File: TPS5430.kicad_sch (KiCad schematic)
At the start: 41 parts, among them J1 Barrel_Jack, J2 Screw_Terminal_01x02, Q1 AO3401A, Q2 MMBT3904, U1 TPS5430DDA

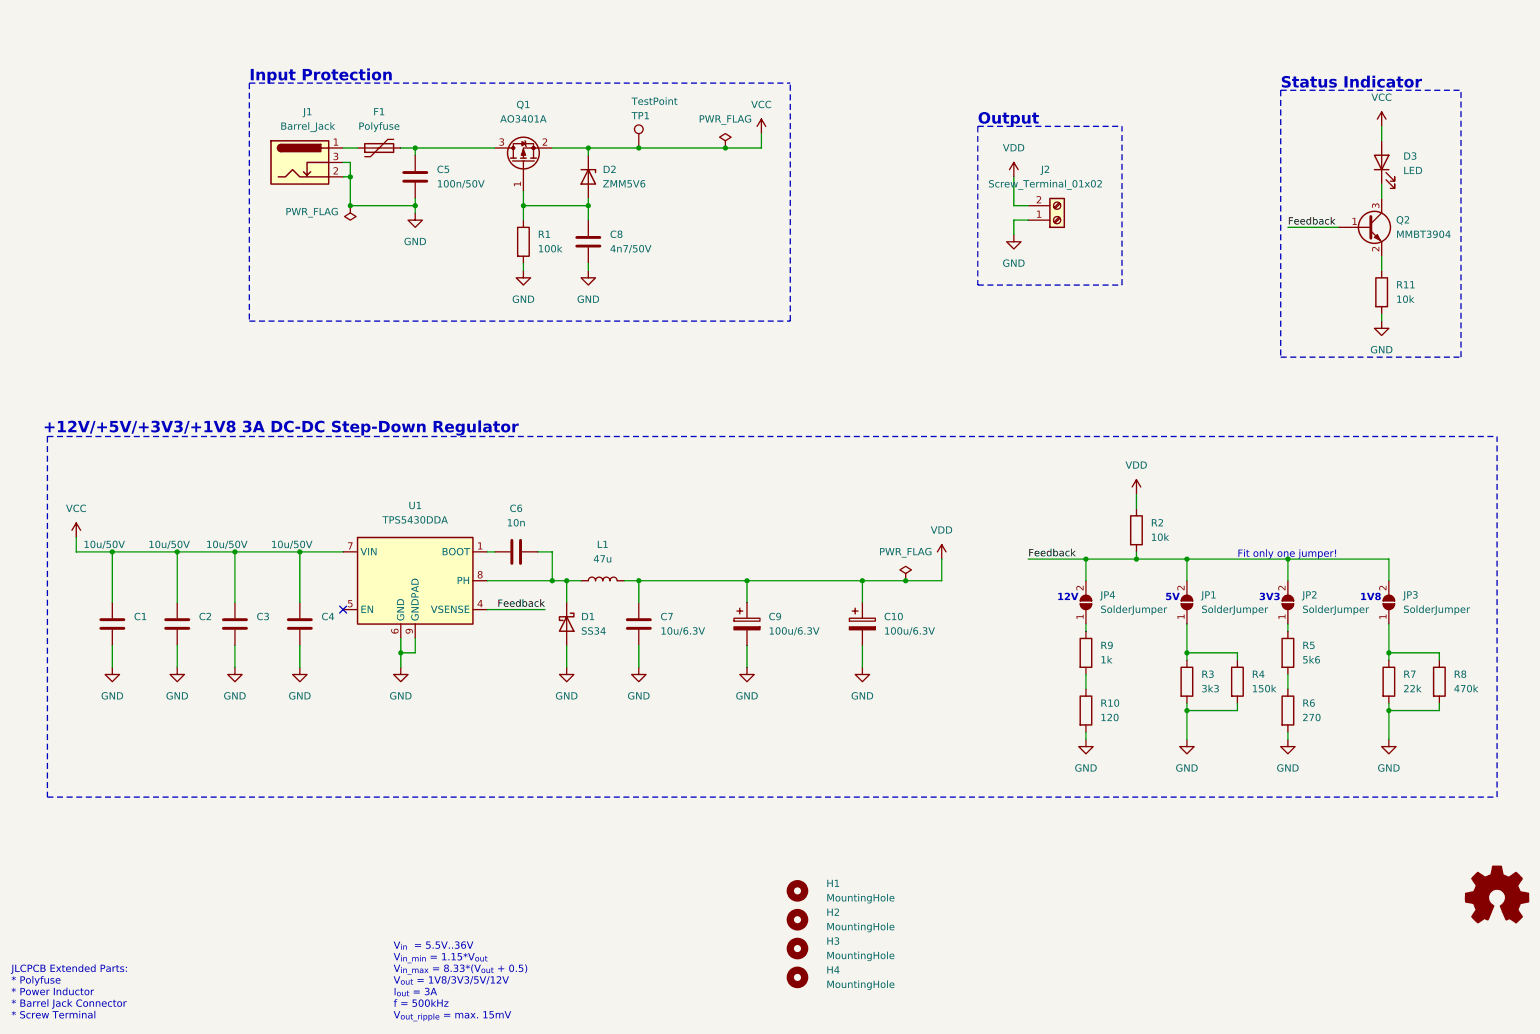
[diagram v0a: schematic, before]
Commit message: Initial addition of variable feedback block
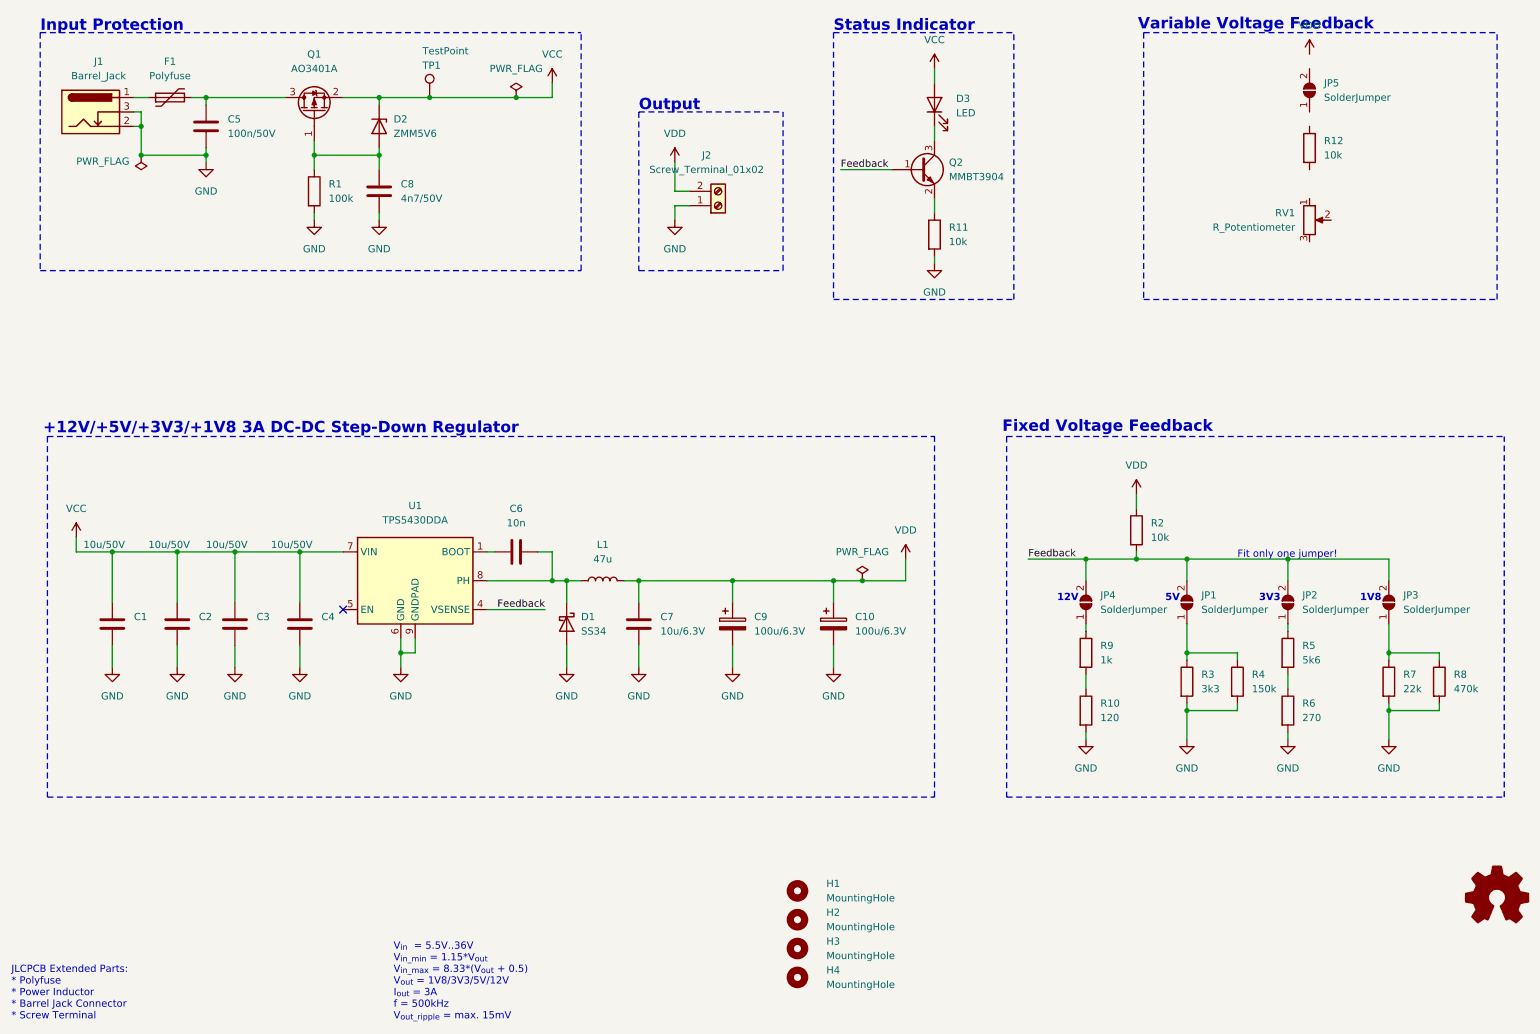
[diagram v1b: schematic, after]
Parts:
- added JP5: SolderJumper, Jumper:SolderJumper-2_P1.3mm_Open_RoundedPad1.0x1.5mm, symbol Jumper:SolderJumper_2_Open
- added R12: 10k, Resistor_SMD:R_0402_1005Metric, symbol Device:R
- added RV1: R_Potentiometer, Potentiometer_THT:Potentiometer_Bourns_3296W_Vertical, symbol Device:R_Potentiometer
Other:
- note added: "Fixed Voltage Feedback"
- note added: "Variable Voltage Feedback"
- company: Max Stabel -> Oren's Lab
- title: TPS5430 -> tps5430-variable
- moved on the sheet: C10, C5, C8, C9, D2, D3, F1, J1, J2, Q1, Q2, R1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

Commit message: Finished variable feedback block
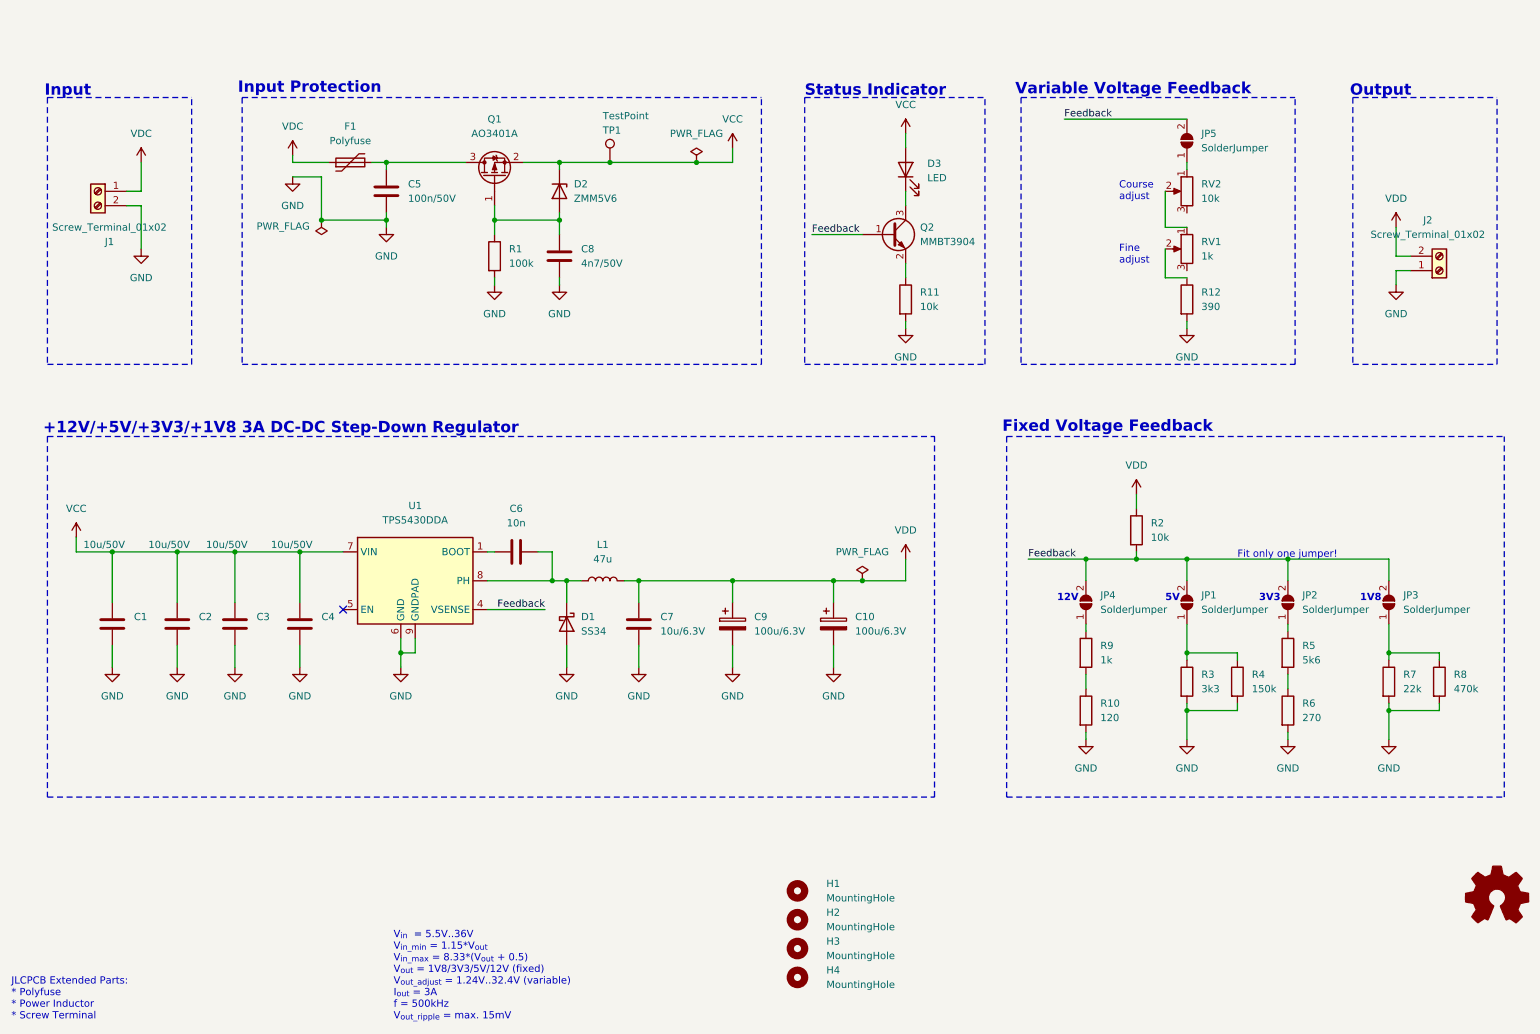
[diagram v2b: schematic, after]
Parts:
- removed J1: Barrel_Jack, tps5430:DC-005-5A-2.0-SMT, symbol Connector:Barrel_Jack_Switch
- added J1: Screw_Terminal_01x02, TerminalBlock_Phoenix:TerminalBlock_Phoenix_PT-1,5-2-3.5-H_1x02_P3.50mm_Horizontal, symbol Connector:Screw_Terminal_01x02
- added RV2: 10k, Potentiometer_THT:Potentiometer_Bourns_3296W_Vertical, symbol Device:R_Potentiometer
- R12: value 10k -> 390; footprint Resistor_SMD:R_0402_1005Metric -> Resistor_SMD:R_0603_1608Metric; JLC 0402 -> 0603; LCSC C25744 -> C22966; MPN 0402WGF1002TCE -> 0603WAF2700T5E; Notes 10kΩ ±1% 1/16W ±100ppm/℃ 0402 Chip Resistor - Surface Mount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 -> 270Ω ±1% 0.1W ±100ppm/℃ 0603 Chip Resistor - Surface Mount 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
- RV1: value R_Potentiometer -> 1k
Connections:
- net Feedback: now also JP5.2 (B)
- net GND: now also R12.2, J1.2 (Pin_2)
- net VDC: now reaches F1.1
- net VDC: now also J1.1 (Pin_1)
- net at R12.1: now also RV1.2
- net at RV1.1: now also RV2.2
- net at JP5.1 (A): now also RV2.1
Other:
- note added: "Course adjust"
- note added: "Fine adjust"
- note added: "Input"
- note added: "JLCPCB Extended Parts: * Polyfuse * Power Inductor * Screw Terminal"
- note added: "V_{in} = 5.5V..36V V_{in_min} = 1.15*V_{out} V_{in_max} = 8.33*(V_{out} + 0.5) V_{out} = 1V8/3V3/5V/12V (fixed) V_{out_adjust} = 1.24V..32.4V (variable) I_{out} = 3A f = 500kHz V_{out_ripple} = max. 15mV"
- note removed: "JLCPCB Extended Parts: * Polyfuse * Power Inductor * Barrel Jack Connector * Screw Terminal"
- note removed: "V_{in} = 5.5V..36V V_{in_min} = 1.15*V_{out} V_{in_max} = 8.33*(V_{out} + 0.5) V_{out} = 1V8/3V3/5V/12V I_{out} = 3A f = 500kHz V_{out_ripple} = max. 15mV"
- moved on the sheet: C5, C8, D2, D3, F1, J2, JP5, Q1, Q2, R1, R11, RV1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

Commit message: Completed placement and routing; Updated REAMME and docs
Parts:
- renumbered JP3 to JP1, JP1 to JP3
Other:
- note added: "VAR"
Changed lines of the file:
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@@
 		)
 	)
+	(text "VAR"
+		(exclude_from_sim no)
+		(at 216.916 40.894 0)
+		(effects
+			(font
+				(size 1.27 1.27)
+				(thickness 0.254)
+				(bold yes)
+			)
+			(justify left bottom)
+		)
+	)
 	(text "5V"
 		(exclude_from_sim no)
@@
 	)
 	(symbol
+		(lib_name "VDD_2")
 		(lib_id "power:VDD")
 		(at 213.36 102.87 0)
@@
 	)
 	(symbol
+		(lib_name "GND_18")
 		(lib_id "power:GND")
 		(at 44.45 133.35 0)
@@
 	)
 	(symbol
+		(lib_name "VCC_1")
 		(lib_id "power:VCC")
 		(at 26.67 110.49 0)
@@
 	)
 	(symbol
+		(lib_name "PWR_FLAG_1")
 		(lib_id "power:PWR_FLAG")
 		(at 69.85 54.61 180)
@@
 	)
 	(symbol
+		(lib_name "GND_20")
 		(lib_id "power:GND")
 		(at 64.77 46.99 0)
@@
 	)
 	(symbol
+		(lib_name "MountingHole_1")
 		(lib_id "Mechanical:MountingHole")
 		(at 153.67 177.8 270)
@@
 	)
 	(symbol
+		(lib_name "GND_19")
 		(lib_id "power:GND")
 		(at 204.47 146.05 0)
@@
 	)
 	(symbol
+		(lib_name "SolderJumper_2_Open_4")
 		(lib_id "Jumper:SolderJumper_2_Open")
 		(at 257.81 121.92 90)
@@
 		(dnp no)
 		(fields_autoplaced yes)
-		(property "Reference" "JP3"
+		(property "Reference" "JP1"
 			(at 260.35 120.6499 90)
 			(effects
@@
 			(project ""
 				(path "/c0e520e3-a475-445c-acca-7b616a001972"
-					(reference "JP3")
+					(reference "JP1")
 					(unit 1)
 				)
@@
 	)
 	(symbol
+		(lib_name "PWR_FLAG_2")
 		(lib_id "power:PWR_FLAG")
 		(at 165.1 118.11 0)
@@
 	)
 	(symbol
+		(lib_name "GND_2")
 		(lib_id "power:GND")
 		(at 81.28 55.88 0)
@@
 	)
 	(symbol
+		(lib_name "GND_11")
 		(lib_id "power:GND")
 		(at 222.25 146.05 0)
@@
 	)
 	(symbol
+		(lib_name "GND_10")
 		(lib_id "power:GND")
 		(at 38.1 59.69 0)
@@
 	)
 	(symbol
+		(lib_name "GND_9")
 		(lib_id "power:GND")
 		(at 33.02 133.35 0)
@@
 	)
 	(symbol
+		(lib_name "MountingHole_2")
 		(lib_id "Mechanical:MountingHole")
 		(at 153.67 182.88 270)
@@
 	)
 	(symbol
+		(lib_name "GND_8")
 		(lib_id "power:GND")
 		(at 113.03 133.35 0)
@@
 	)
 	(symbol
+		(lib_name "GND_7")
 		(lib_id "power:GND")
 		(at 172.72 73.66 0)
@@
 	)
 	(symbol
+		(lib_name "SolderJumper_2_Open_1")
 		(lib_id "Jumper:SolderJumper_2_Open")
 		(at 222.25 121.92 90)
@@
 		(dnp no)
 		(fields_autoplaced yes)
-		(property "Reference" "JP1"
+		(property "Reference" "JP3"
 			(at 224.79 120.6499 90)
 			(effects
@@
 			(project ""
 				(path "/c0e520e3-a475-445c-acca-7b616a001972"
-					(reference "JP1")
+					(reference "JP3")
 					(unit 1)
 				)
@@
 	)
 	(symbol
+		(lib_name "GND_6")
 		(lib_id "power:GND")
 		(at 111.76 66.04 0)
@@
 	)
 	(symbol
+		(lib_name "VCC_2")
 		(lib_id "power:VCC")
 		(at 172.72 39.37 0)
@@
 	)
 	(symbol
+		(lib_name "GND_5")
 		(lib_id "power:GND")
 		(at 66.04 133.35 0)
@@
 	)
 	(symbol
+		(lib_name "GND_4")
 		(lib_id "power:GND")
 		(at 257.81 146.05 0)
@@
 	)
 	(symbol
+		(lib_name "GND_3")
 		(lib_id "power:GND")
 		(at 83.82 133.35 0)
@@
 	)
 	(symbol
+		(lib_name "GND_13")
 		(lib_id "power:GND")
 		(at 222.25 73.66 0)
@@
 	)
 	(symbol
+		(lib_name "GND_12")
 		(lib_id "power:GND")
 		(at 100.33 66.04 0)
@@
 	)
 	(symbol
+		(lib_name "SolderJumper_2_Open_2")
+		(lib_id "Jumper:SolderJumper_2_Open")
+		(at 222.25 40.64 90)
+		(unit 1)
+		(exclude_from_sim no)
+		(in_bom yes)
+		(on_board yes)
+		(dnp no)
+		(property "Reference" "JP5"
+			(at 224.79 39.3699 90)
+			(effects
+				(font
+					(size 1.27 1.27)
+				)
+				(justify right)
+			)
+		)
+		(property "Value" "SolderJumper"
+			(at 224.79 41.9099 90)
+			(effects
+				(font
+					(size 1.27 1.27)
+				)
+				(justify right)
+			)
+		)
+		(property "Footprint" "Jumper:SolderJumper-2_P1.3mm_Open_RoundedPad1.0x1.5mm"
+			(at 222.25 40.64 0)
+			(effects
+				(font
+					(size 1.27 1.27)
+				)
+				(hide yes)
+			)
+		)
+		(property "Datasheet" "~"
+			(at 222.25 40.64 0)
+			(effects
+				(font
+					(size 1.27 1.27)
+				)
+				(hide yes)
+			)
+		)
+		(property "Description" ""
+			(at 222.25 40.64 0)
+			(effects
+				(font
+					(size 1.27 1.27)
+				)
+			)
+		)
+		(pin "1"
+		)
+		(pin "2"
+		)
+		(instances
+			(project "TPS5430"
+				(path "/c0e520e3-a475-445c-acca-7b616a001972"
+					(reference "JP5")
+					(unit 1)
+				)
+			)
+		)
+	)
+	(symbol
 		(lib_id "Transistor_FET:AO3401A")
 		(at 100.33 46.99 90)
@@
 	)
 	(symbol
+		(lib_name "MountingHole_3")
 		(lib_id "Mechanical:MountingHole")
 		(at 153.67 187.96 270)
@@
 	)
 	(symbol
+		(lib_name "GND_15")
 		(lib_id "power:GND")
 		(at 125.73 133.35 0)
@@
 	)
 	(symbol
+		(lib_name "GND_14")
 		(lib_id "power:GND")
 		(at 160.02 133.35 0)
@@
 	)
 	(symbol
+		(lib_name "SolderJumper_2_Open_2")
 		(lib_id "Jumper:SolderJumper_2_Open")
 		(at 204.47 121.92 90)
@@
 	)
 	(symbol
+		(lib_name "GND_17")
 		(lib_id "power:GND")
 		(at 259.08 66.04 0)
@@
 	)
 	(symbol
+		(lib_name "VDD_1")
 		(lib_id "power:VDD")
 		(at 172.72 114.3 0)
@@
 	)
 	(symbol
-		(lib_id "Jumper:SolderJumper_2_Open")
-		(at 222.25 40.64 90)
-		(unit 1)
-		(exclude_from_sim no)
-		(in_bom yes)
-		(on_board yes)
-		(dnp no)
-		(property "Reference" "JP5"
-			(at 224.79 39.3699 90)
-			(effects
-				(font
-					(size 1.27 1.27)
-				)
-				(justify right)
-			)
-		)
-		(property "Value" "SolderJumper"
-			(at 224.79 41.9099 90)
-			(effects
-				(font
-					(size 1.27 1.27)
-				)
-				(justify right)
-			)
-		)
-		(property "Footprint" "Jumper:SolderJumper-2_P1.3mm_Open_RoundedPad1.0x1.5mm"
-			(at 222.25 40.64 0)
-			(effects
-				(font
-					(size 1.27 1.27)
-				)
-				(hide yes)
-			)
-		)
-		(property "Datasheet" "~"
-			(at 222.25 40.64 0)
-			(effects
-				(font
-					(size 1.27 1.27)
-				)
-				(hide yes)
-			)
-		)
-		(property "Description" ""
-			(at 222.25 40.64 0)
-			(effects
-				(font
-					(size 1.27 1.27)
-				)
-			)
-		)
-		(pin "1"
-		)
-		(pin "2"
-		)
-		(instances
-			(project "TPS5430"
-				(path "/c0e520e3-a475-445c-acca-7b616a001972"
-					(reference "JP5")
-					(unit 1)
-				)
-			)
-		)
-	)
-	(symbol
 		(lib_id "power:VCC")
 		(at 142.24 41.91 0)
@@
 	)
 	(symbol
+		(lib_name "GND_16")
 		(lib_id "power:GND")
 		(at 142.24 133.35 0)
@@
 	)
 	(symbol
+		(lib_name "GND_1")
 		(lib_id "power:GND")
 		(at 54.61 133.35 0)

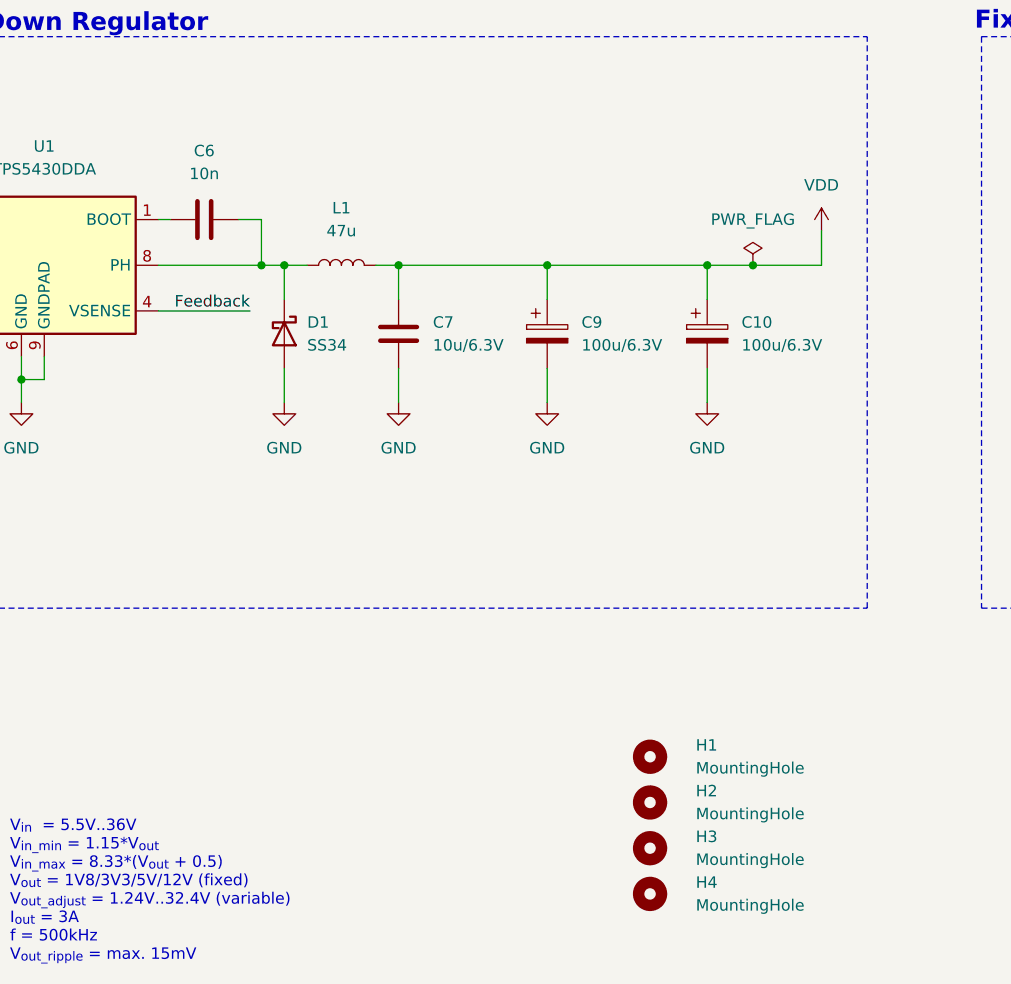
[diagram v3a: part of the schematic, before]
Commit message: printed PCB updates
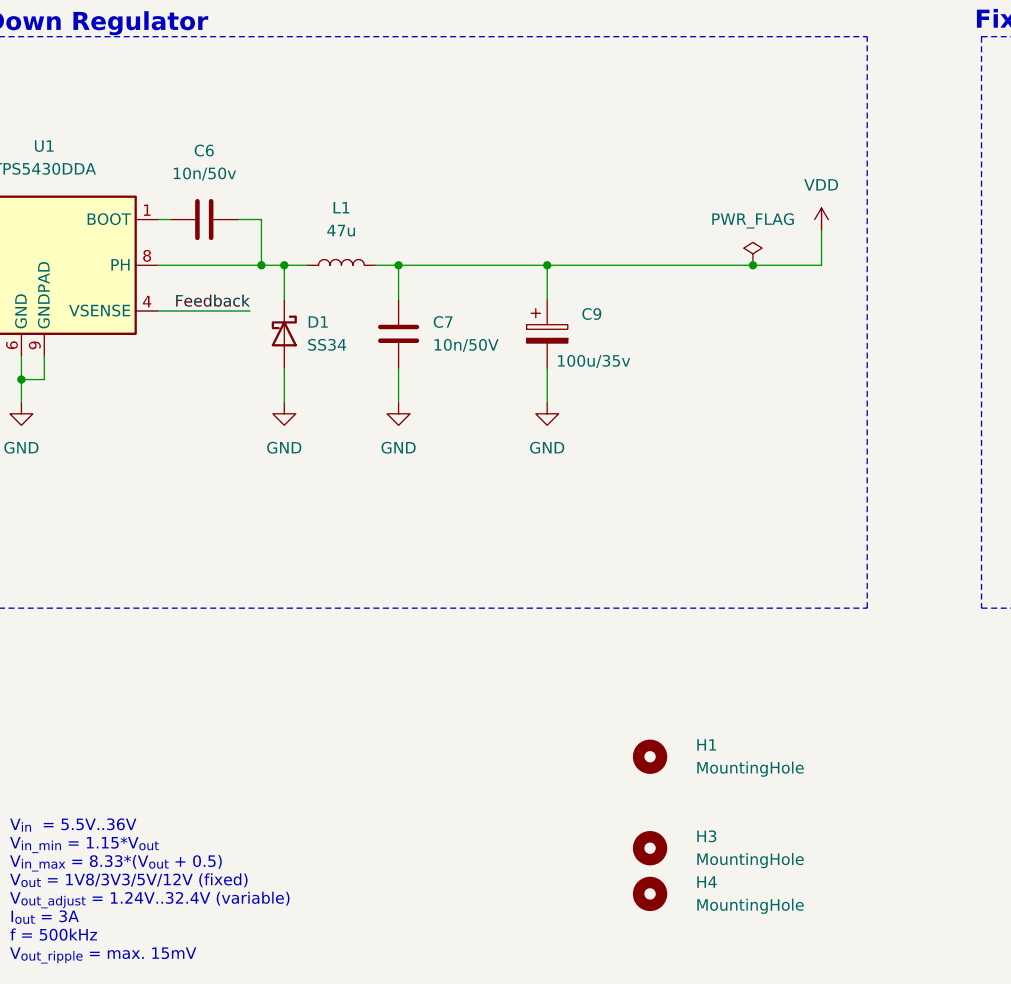
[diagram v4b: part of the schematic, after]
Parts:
- removed C10: 100u/6.3V, Capacitor_Tantalum_SMD:CP_EIA-3528-21_Kemet-B, symbol Device:C_Polarized
- removed H2: MountingHole, MountingHole:MountingHole_2.2mm_M2_ISO7380, symbol Mechanical:MountingHole
- C6: value 10n -> 10n/50v
- C7: value 10u/6.3V -> 10n/50V
- C9: value 100u/6.3V -> 100u/35v; footprint Capacitor_Tantalum_SMD:CP_EIA-3528-21_Kemet-B -> Capacitor_Tantalum_SMD:CP_EIA-7343-43_Kemet-X
